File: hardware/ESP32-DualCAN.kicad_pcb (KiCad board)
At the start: 2 copper layers, 38.8 x 19.6 mm, 28 parts, among them J1 Molex 70553 6p, J2 Conn_01x10_Socket, J3 Conn_01x10_Socket, J4 holes, J5 pads, J6 holes, J7 pads, U1 LV2862Y, U2 ESP32-C6-SuperMini, U3 TCAN1044AV, U4 TCAN1044AV

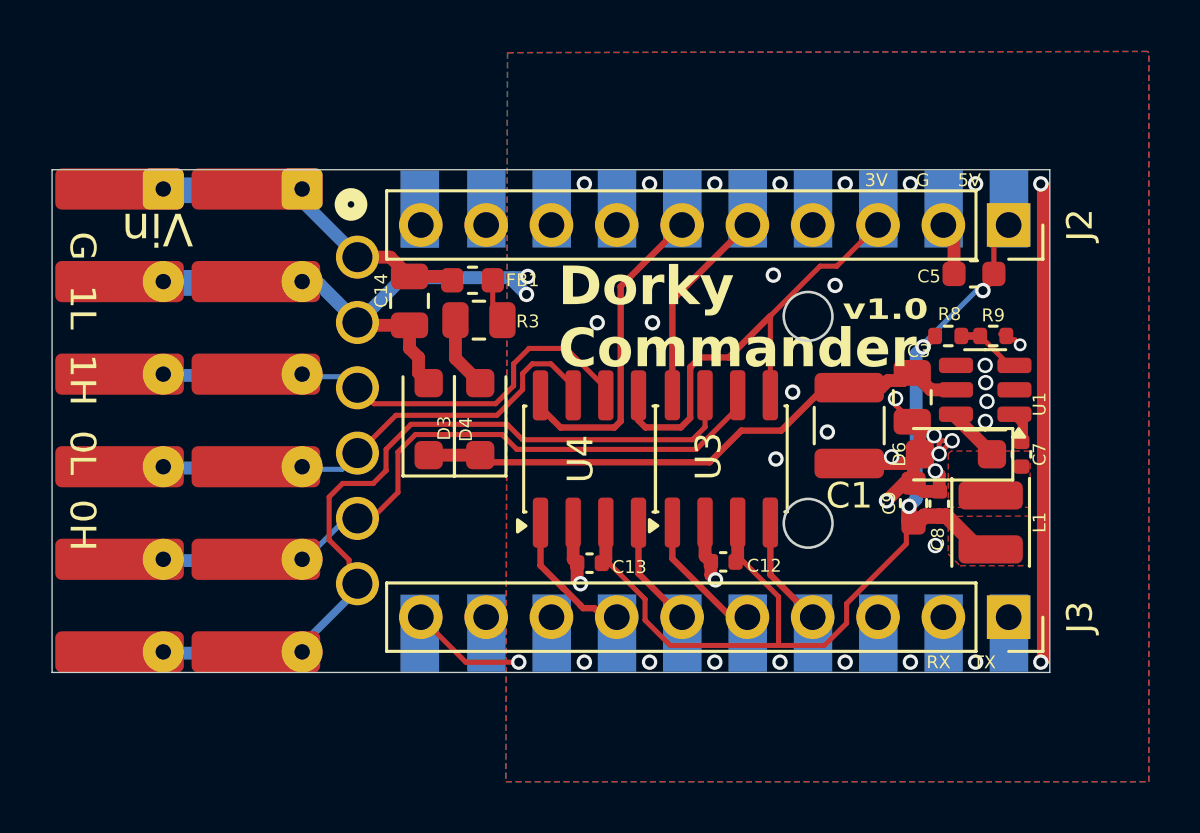
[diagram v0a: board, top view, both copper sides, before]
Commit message: Use 8MB ESP32-C6-Zero
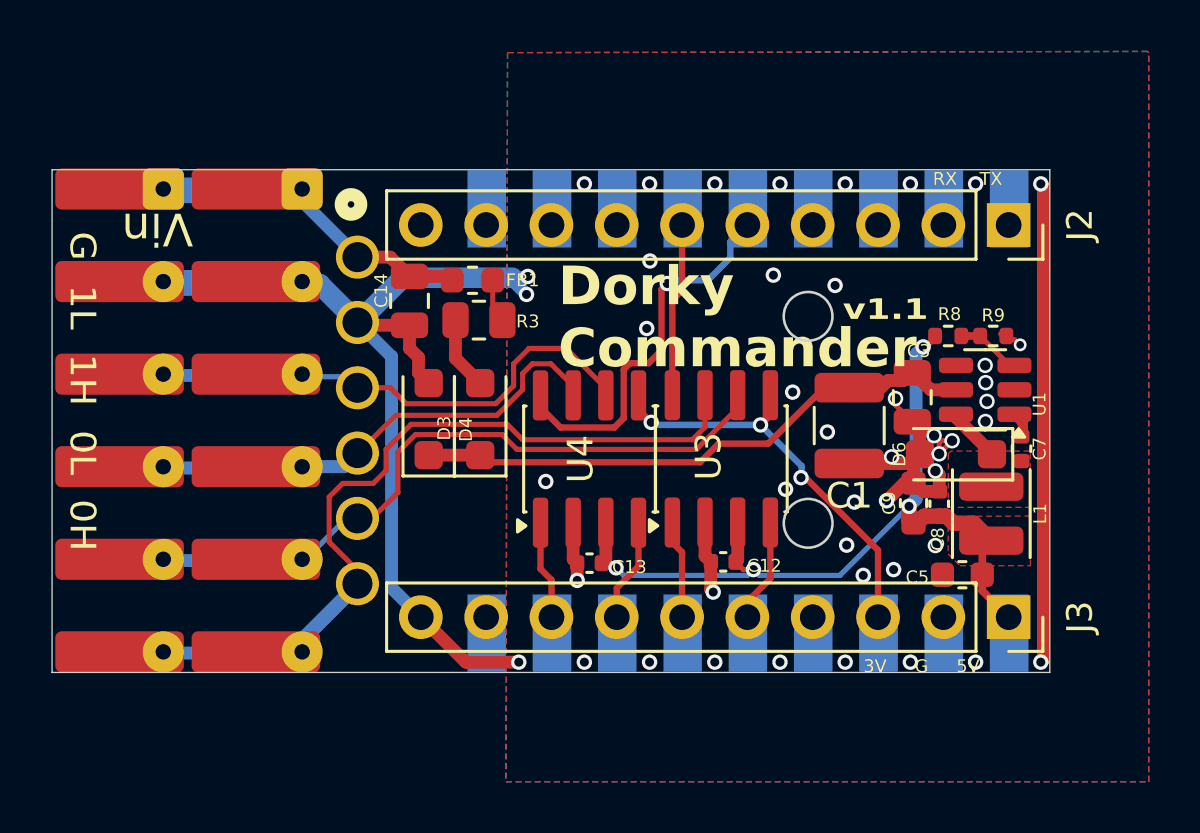
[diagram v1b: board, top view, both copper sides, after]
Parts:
- removed U2: ESP32-C6-SuperMini, lib:ESP32-C6-SuperMini
- added U5: ESP32-C6-Zero, Waveshare-ESP32:Waveshare-ESP32-C6-Zero, B.Cu at (149.0, 91.1)
- moved C5 11.7 mm to (157.1, 96.6)
- moved L1 0.34 mm to (158.2, 94.2)
- moved C7 0.22 mm to (159.3, 91.7)
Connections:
- J2 pad 1: +5V -> Net-(J2-Pin_1)
- J2 pad 10: Net-(J2-Pin_10) -> unconnected-(J2-Pin_10-Pad10)
- J2 pad 2: GND -> Net-(J2-Pin_2)
- J2 pad 3: +3.3V -> Net-(J2-Pin_3)
- J2 pad 5: CAN0_RS -> CAN1_RS
- J2 pad 6: CAN1_RS -> CAN0_RS
- J3 pad 1: Net-(J3-Pin_1) -> +5V
- J3 pad 2: Net-(J3-Pin_2) -> GND
- J3 pad 3: Net-(J3-Pin_3) -> +3.3V
- J3 pad 4: CAN0_RXD -> Net-(J3-Pin_4)
- J3 pad 5: CAN0_TXD -> CAN0_RXD
- J3 pad 6: CAN1_RXD -> CAN0_TXD
- J3 pad 7: CAN1_TXD -> CAN1_RXD
- J3 pad 8: Net-(J3-Pin_8) -> CAN1_TXD
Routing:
- net GND: track 67.0 -> 77.7 mm, vias 41 -> 46
- net +5V: track 43.0 -> 33.8 mm, vias 3 -> 4
- net CAN0_H: track 30.6 -> 34.3 mm
- net CAN1_H: track 18.7 -> 21.1 mm
- net CAN1_RS: track 12.6 -> 15.0 mm, vias 0 -> 1
- net CAN1_TXD: track 5.47 -> 3.85 mm
- net +3.3V: track 17.9 -> 16.3 mm, vias 0 -> 3
- net CAN0_TXD: track 5.26 -> 3.84 mm
- net CAN0_RS: track 7.83 -> 6.78 mm

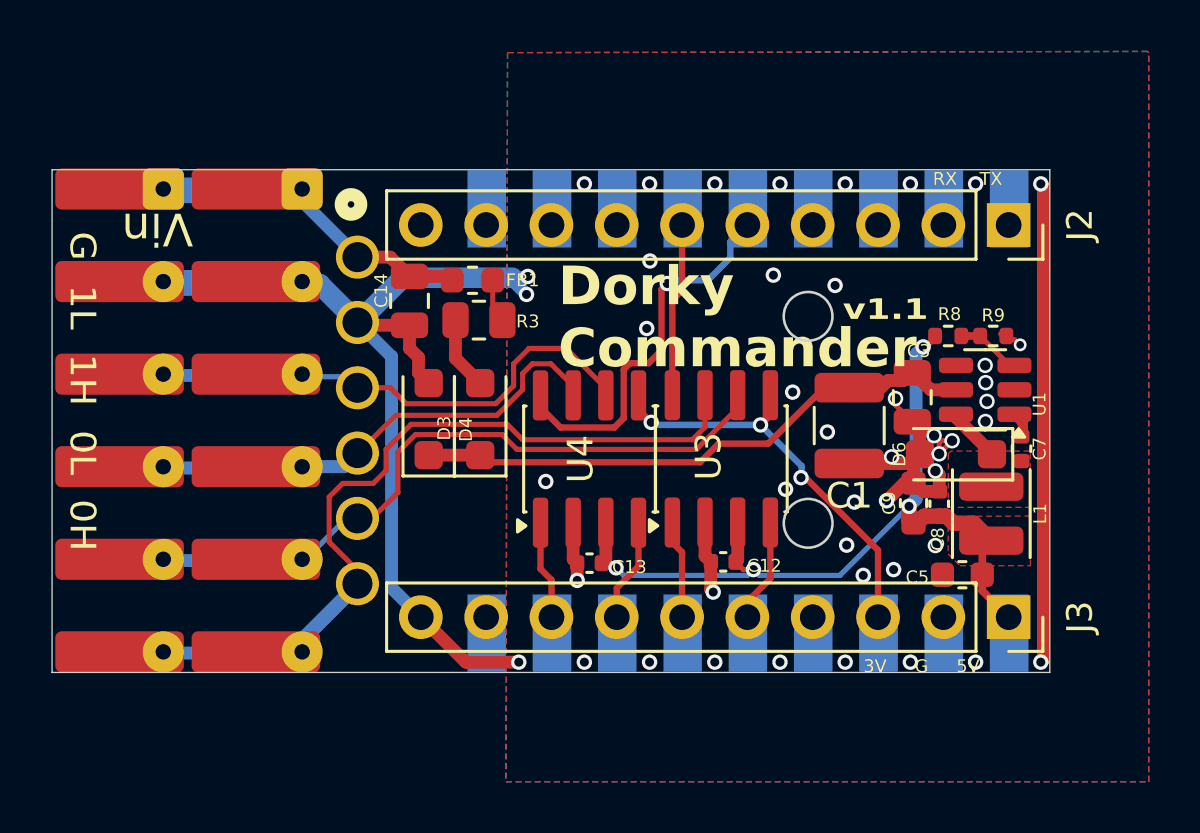
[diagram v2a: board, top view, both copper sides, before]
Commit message: DNP input filtering.  Changed vout resistors
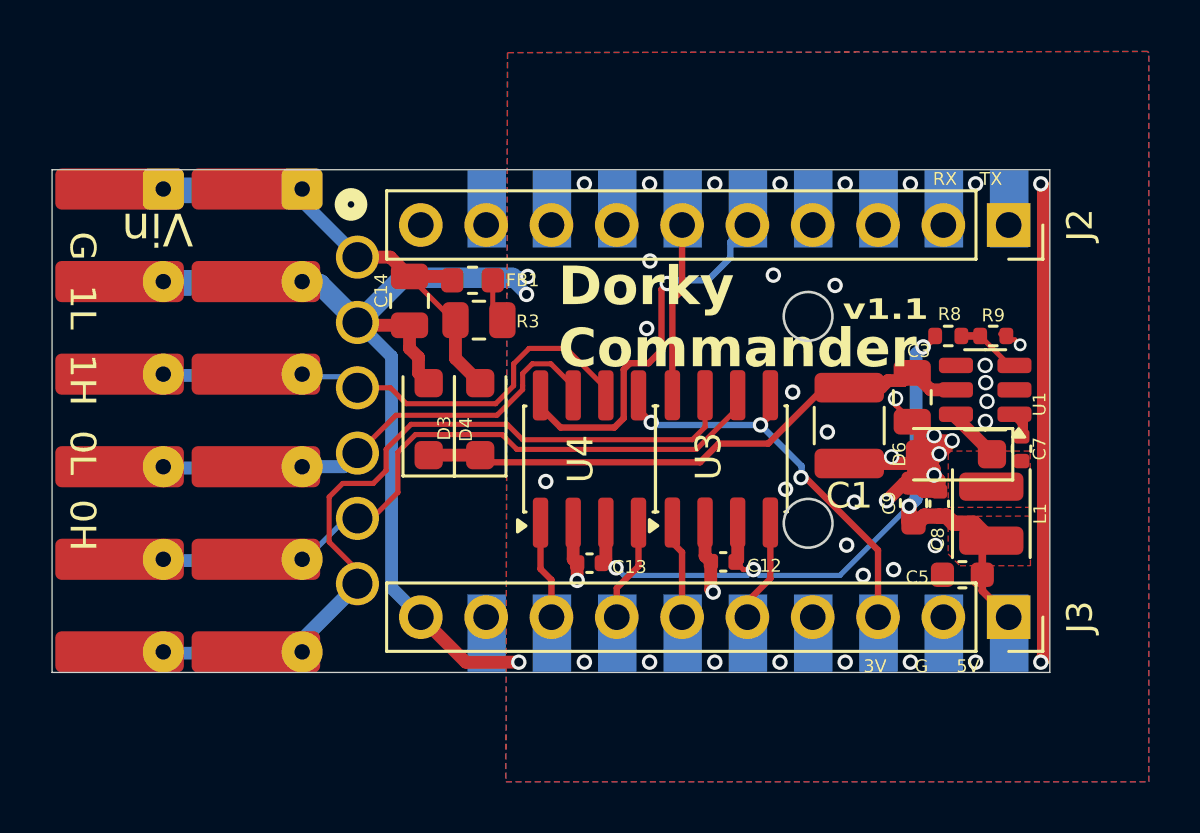
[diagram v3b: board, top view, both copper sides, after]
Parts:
- R8: value 68k -> 56k
- R9: value 12k -> 10k
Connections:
- D3 pad 2: Net-(D3-A) -> +BATT
- R3 pad 2: Net-(D3-A) -> +BATT
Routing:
- net +BATT: track 13.1 -> 18.5 mm
- net GND: track 77.7 -> 82.0 mm
- net Net-(D3-A): track 2.85 -> 0.00 mm

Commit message: cheaper parts, tooling holes
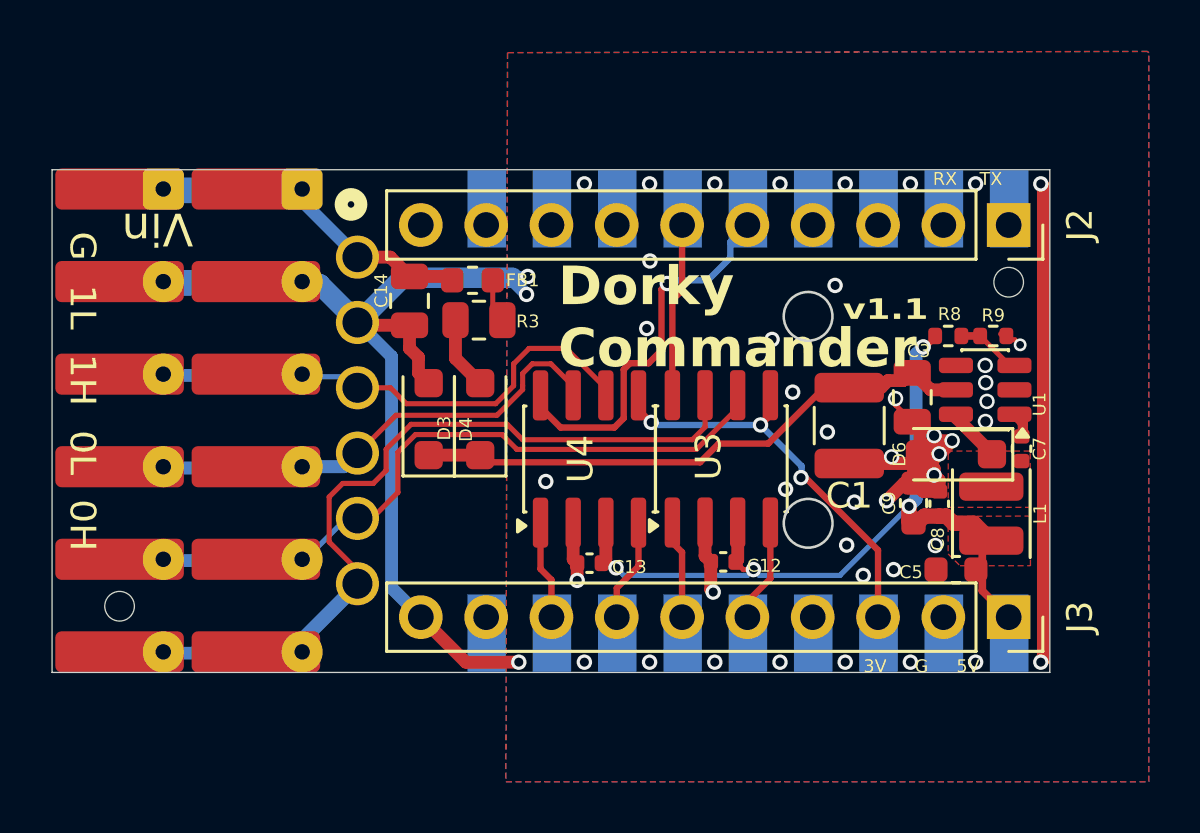
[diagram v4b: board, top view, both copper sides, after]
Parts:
- added ?: JLCPCB_ToolingHole, part:JLCPCB_ToolingHole, F.Cu at (124.3, 97.8)
- added ?: JLCPCB_ToolingHole, part:JLCPCB_ToolingHole, F.Cu at (158.8, 85.2)
- moved C5 0.32 mm to (156.8, 96.4)
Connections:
- D3 pad 2: +BATT -> unconnected-(D3-A-Pad2)
- R3 pad 2: +BATT -> unconnected-(D3-A-Pad2)
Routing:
- net +BATT: track 18.5 -> 13.1 mm
- net unconnected-(D3-A-Pad2): track 0.00 -> 2.94 mm
